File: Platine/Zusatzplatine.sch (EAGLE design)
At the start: 23 parts

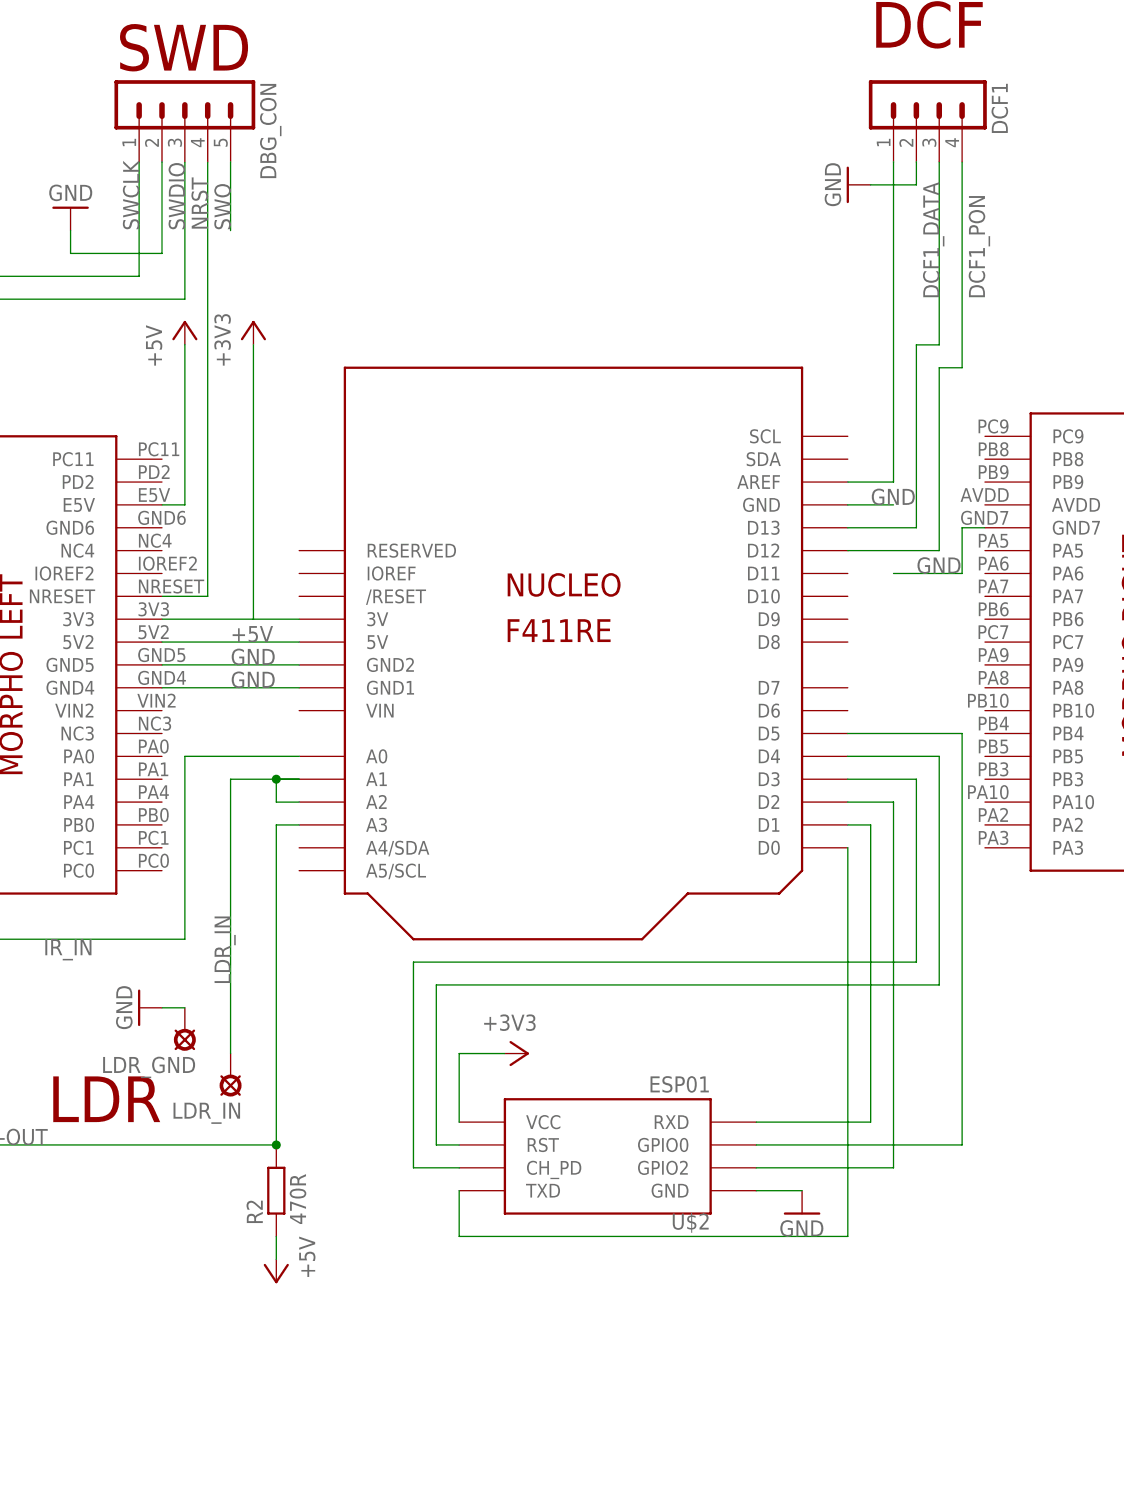
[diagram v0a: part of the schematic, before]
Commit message: Added Upside Down Mount Option for WiFI Improved Documentation on Board
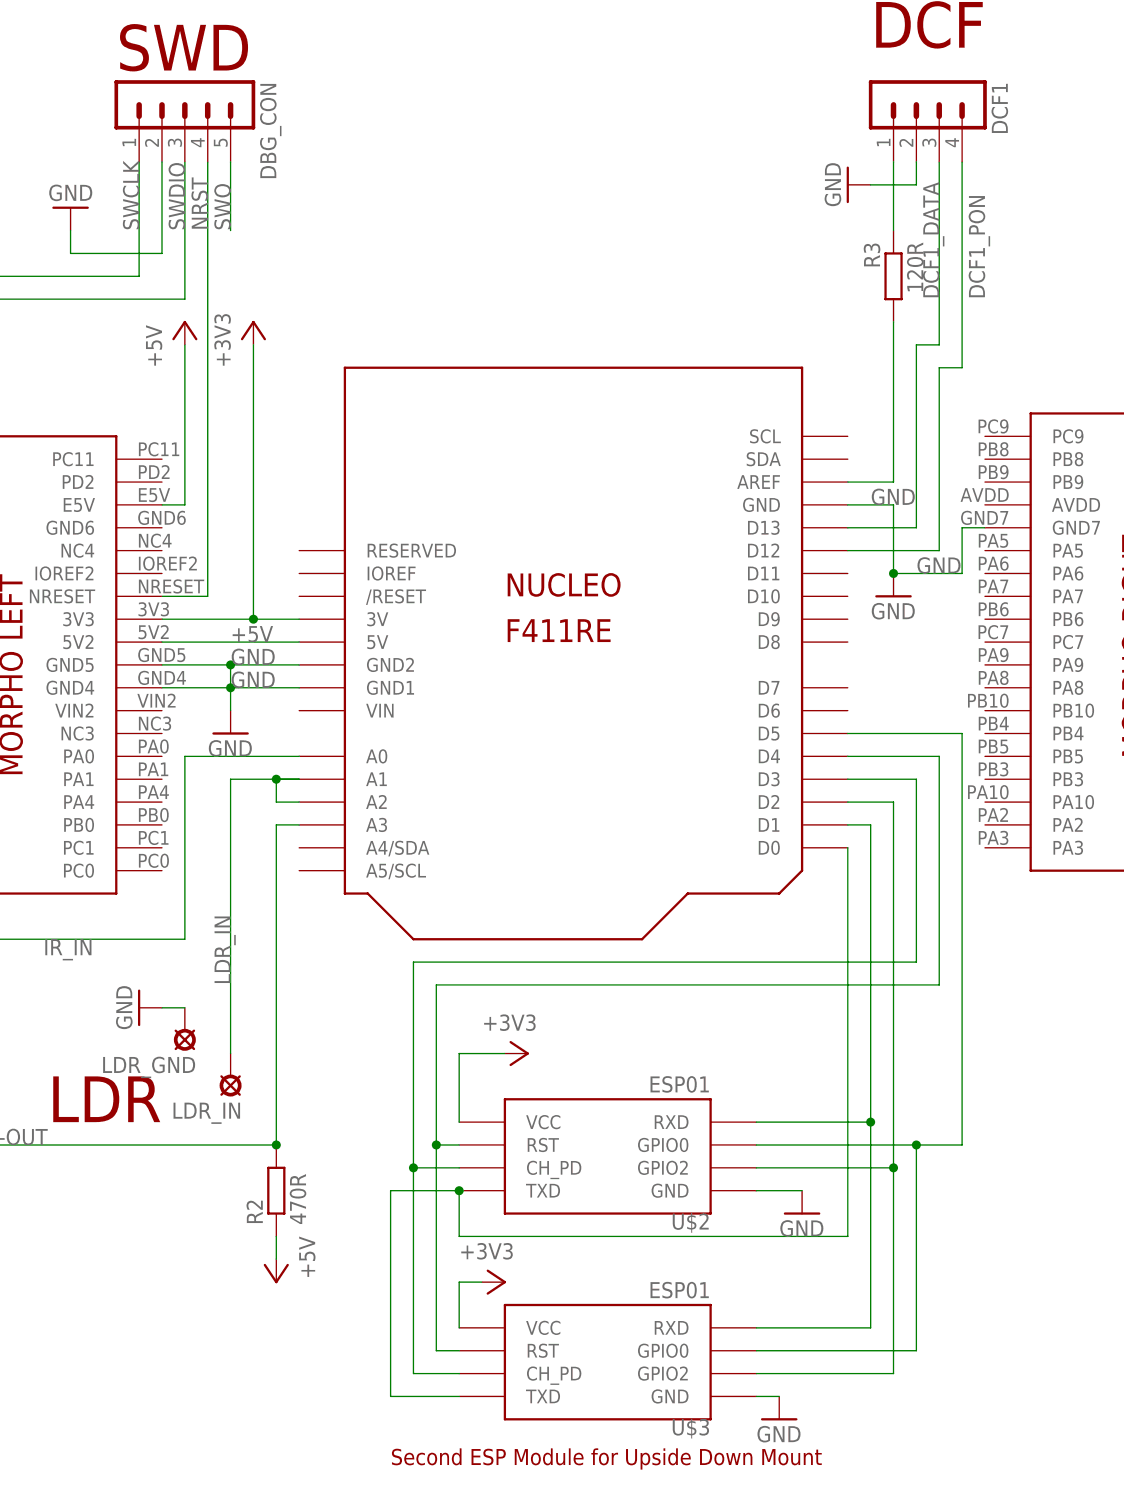
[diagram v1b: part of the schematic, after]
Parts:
- added R3: 120R, rcl:R-EU_R1206
- added U$3: ESP01, esp8266modules:ESP01
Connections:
- new net N$2: DCF1.1, R3.1
- net +3V3: now also U$3.VCC
- net GND: now also U$3.GND
- net N$1: now also R3.2; no longer DCF1.1
- net N$12: now also U$3.GPIO0
- net N$13: now also U$3.RST
- net N$14: now also U$3.CH_PD
- net N$15: now also U$3.TXD
- net N$16: now also U$3.RXD
- net N$17: now also U$3.GPIO2
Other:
- note added: "Second ESP Module for Upside Down Mount"
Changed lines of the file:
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@@
 <part name="GND6" library="supply1" deviceset="GND" device=""/>
 <part name="3V3" library="supply1" deviceset="+3V3" device=""/>
+<part name="U$3" library="esp8266modules" deviceset="ESP01" device=""/>
+<part name="3V4" library="supply1" deviceset="+3V3" device=""/>
+<part name="GND7" library="supply1" deviceset="GND" device=""/>
+<part name="GND8" library="supply1" deviceset="GND" device=""/>
+<part name="GND9" library="supply1" deviceset="GND" device=""/>
+<part name="R3" library="rcl" deviceset="R-EU_" device="R1206" value="120R"/>
 </parts>
 <sheets>
@@
 <text x="-50.8" y="-165.1" size="5.08" layer="94">IR</text>
 <text x="-20.32" y="-48.26" size="5.08" layer="94">SWD</text>
+<text x="10.16" y="-203.2" size="1.778" layer="94">Second ESP Module for Upside Down Mount</text>
 </plain>
 <instances>
@@
 <instance part="GND6" gate="1" x="-25.4" y="-63.5" rot="R180"/>
 <instance part="3V3" gate="G$1" x="25.4" y="-157.48" rot="R270"/>
+<instance part="U$3" gate="G$1" x="33.02" y="-187.96" rot="R180"/>
+<instance part="3V4" gate="G$1" x="22.86" y="-182.88" rot="R270"/>
+<instance part="GND7" gate="1" x="53.34" y="-198.12"/>
+<instance part="GND8" gate="1" x="-7.62" y="-121.92"/>
+<instance part="GND9" gate="1" x="66.04" y="-106.68"/>
+<instance part="R3" gate="G$1" x="66.04" y="-71.12" rot="MR270"/>
 </instances>
 <busses>
@@
 </segment>
 <segment>
+<pinref part="U$1" gate="G$1" pin="GND1"/>
+<pinref part="U$1" gate="G$1" pin="GND4"/>
+<wire x1="0" y1="-116.84" x2="-7.62" y2="-116.84" width="0.1524" layer="91"/>
+<label x="-7.62" y="-116.84" size="1.778" layer="95"/>
+<pinref part="GND8" gate="1" pin="GND"/>
+<wire x1="-7.62" y1="-116.84" x2="-15.24" y2="-116.84" width="0.1524" layer="91"/>
+<wire x1="-7.62" y1="-119.38" x2="-7.62" y2="-116.84" width="0.1524" layer="91"/>
 <pinref part="U$1" gate="G$1" pin="GND2"/>
 <pinref part="U$1" gate="G$1" pin="GND5"/>
-<wire x1="0" y1="-114.3" x2="-15.24" y2="-114.3" width="0.1524" layer="91"/>
+<wire x1="0" y1="-114.3" x2="-7.62" y2="-114.3" width="0.1524" layer="91"/>
 <label x="-7.62" y="-114.3" size="1.778" layer="95"/>
-</segment>
-<segment>
-<pinref part="U$1" gate="G$1" pin="GND1"/>
-<pinref part="U$1" gate="G$1" pin="GND4"/>
-<wire x1="0" y1="-116.84" x2="-15.24" y2="-116.84" width="0.1524" layer="91"/>
-<label x="-7.62" y="-116.84" size="1.778" layer="95"/>
+<wire x1="-7.62" y1="-114.3" x2="-15.24" y2="-114.3" width="0.1524" layer="91"/>
+<wire x1="-7.62" y1="-116.84" x2="-7.62" y2="-114.3" width="0.1524" layer="91"/>
+<junction x="-7.62" y="-116.84"/>
+<junction x="-7.62" y="-114.3"/>
 </segment>
 <segment>
@@
 <wire x1="73.66" y1="-104.14" x2="66.04" y2="-104.14" width="0.1524" layer="91"/>
 <label x="68.58" y="-104.14" size="1.778" layer="95"/>
-</segment>
-<segment>
+<pinref part="GND9" gate="1" pin="GND"/>
 <pinref part="U$1" gate="G$1" pin="GND"/>
 <wire x1="60.96" y1="-96.52" x2="66.04" y2="-96.52" width="0.1524" layer="91"/>
 <label x="63.5" y="-96.52" size="1.778" layer="95"/>
+<wire x1="66.04" y1="-96.52" x2="66.04" y2="-104.14" width="0.1524" layer="91"/>
+<junction x="66.04" y="-104.14"/>
+</segment>
+<segment>
+<pinref part="U$3" gate="G$1" pin="GND"/>
+<pinref part="GND7" gate="1" pin="GND"/>
+<wire x1="50.8" y1="-195.58" x2="53.34" y2="-195.58" width="0.1524" layer="91"/>
 </segment>
 </net>
@@
 <segment>
 <pinref part="U$2" gate="G$1" pin="GPIO0"/>
-<wire x1="50.8" y1="-167.64" x2="73.66" y2="-167.64" width="0.1524" layer="91"/>
+<wire x1="50.8" y1="-167.64" x2="68.58" y2="-167.64" width="0.1524" layer="91"/>
+<wire x1="68.58" y1="-167.64" x2="73.66" y2="-167.64" width="0.1524" layer="91"/>
 <wire x1="73.66" y1="-167.64" x2="73.66" y2="-121.92" width="0.1524" layer="91"/>
 <pinref part="U$1" gate="G$1" pin="D5"/>
 <wire x1="73.66" y1="-121.92" x2="60.96" y2="-121.92" width="0.1524" layer="91"/>
+<pinref part="U$3" gate="G$1" pin="GPIO0"/>
+<wire x1="50.8" y1="-190.5" x2="68.58" y2="-190.5" width="0.1524" layer="91"/>
+<wire x1="68.58" y1="-190.5" x2="68.58" y2="-167.64" width="0.1524" layer="91"/>
+<junction x="68.58" y="-167.64"/>
 </segment>
 </net>
@@
 <pinref part="U$1" gate="G$1" pin="D4"/>
 <wire x1="71.12" y1="-124.46" x2="60.96" y2="-124.46" width="0.1524" layer="91"/>
+<wire x1="15.24" y1="-167.64" x2="15.24" y2="-190.5" width="0.1524" layer="91"/>
+<pinref part="U$3" gate="G$1" pin="RST"/>
+<wire x1="15.24" y1="-190.5" x2="17.78" y2="-190.5" width="0.1524" layer="91"/>
+<junction x="15.24" y="-167.64"/>
 </segment>
 </net>
@@
 <pinref part="U$1" gate="G$1" pin="D3"/>
 <wire x1="68.58" y1="-127" x2="60.96" y2="-127" width="0.1524" layer="91"/>
+<wire x1="12.7" y1="-170.18" x2="12.7" y2="-193.04" width="0.1524" layer="91"/>
+<pinref part="U$3" gate="G$1" pin="CH_PD"/>
+<wire x1="12.7" y1="-193.04" x2="17.78" y2="-193.04" width="0.1524" layer="91"/>
+<junction x="12.7" y="-170.18"/>
 </segment>
 </net>
@@
 <wire x1="17.78" y1="-177.8" x2="60.96" y2="-177.8" width="0.1524" layer="91"/>
 <wire x1="60.96" y1="-177.8" x2="60.96" y2="-134.62" width="0.1524" layer="91"/>
+<pinref part="U$3" gate="G$1" pin="TXD"/>
+<wire x1="17.78" y1="-195.58" x2="10.16" y2="-195.58" width="0.1524" layer="91"/>
+<wire x1="10.16" y1="-195.58" x2="10.16" y2="-172.72" width="0.1524" layer="91"/>
+<wire x1="10.16" y1="-172.72" x2="17.78" y2="-172.72" width="0.1524" layer="91"/>
+<junction x="17.78" y="-172.72"/>
 </segment>
 </net>
@@
 <pinref part="U$2" gate="G$1" pin="RXD"/>
 <wire x1="63.5" y1="-165.1" x2="50.8" y2="-165.1" width="0.1524" layer="91"/>
+<pinref part="U$3" gate="G$1" pin="RXD"/>
+<wire x1="50.8" y1="-187.96" x2="63.5" y2="-187.96" width="0.1524" layer="91"/>
+<wire x1="63.5" y1="-187.96" x2="63.5" y2="-165.1" width="0.1524" layer="91"/>
+<junction x="63.5" y="-165.1"/>
 </segment>
 </net>
@@
 <pinref part="U$1" gate="G$1" pin="D2"/>
 <wire x1="66.04" y1="-129.54" x2="60.96" y2="-129.54" width="0.1524" layer="91"/>
+<pinref part="U$3" gate="G$1" pin="GPIO2"/>
+<wire x1="50.8" y1="-193.04" x2="66.04" y2="-193.04" width="0.1524" layer="91"/>
+<wire x1="66.04" y1="-193.04" x2="66.04" y2="-170.18" width="0.1524" layer="91"/>
+<junction x="66.04" y="-170.18"/>
 </segment>
 </net>
@@
 <net name="N$1" class="0">
 <segment>
-<pinref part="DCF1" gate="1" pin="1"/>
-<wire x1="66.04" y1="-58.42" x2="66.04" y2="-93.98" width="0.1524" layer="91"/>
 <pinref part="U$1" gate="G$1" pin="AREF"/>
 <wire x1="66.04" y1="-93.98" x2="60.96" y2="-93.98" width="0.1524" layer="91"/>
+<pinref part="R3" gate="G$1" pin="2"/>
+<wire x1="66.04" y1="-76.2" x2="66.04" y2="-93.98" width="0.1524" layer="91"/>
 </segment>
 </net>
@@
 <pinref part="U$1" gate="G$1" pin="3V"/>
 <wire x1="-5.08" y1="-109.22" x2="0" y2="-109.22" width="0.1524" layer="91"/>
+<junction x="-5.08" y="-109.22"/>
 </segment>
 <segment>
@@
 <pinref part="3V3" gate="G$1" pin="+3V3"/>
 <wire x1="17.78" y1="-157.48" x2="22.86" y2="-157.48" width="0.1524" layer="91"/>
+</segment>
+<segment>
+<pinref part="U$3" gate="G$1" pin="VCC"/>
+<wire x1="17.78" y1="-187.96" x2="17.78" y2="-182.88" width="0.1524" layer="91"/>
+<pinref part="3V4" gate="G$1" pin="+3V3"/>
+<wire x1="17.78" y1="-182.88" x2="20.32" y2="-182.88" width="0.1524" layer="91"/>
 </segment>
 </net>
@@
 </segment>
 </net>
+<net name="N$2" class="0">
+<segment>
+<pinref part="DCF1" gate="1" pin="1"/>
+<pinref part="R3" gate="G$1" pin="1"/>
+<wire x1="66.04" y1="-58.42" x2="66.04" y2="-66.04" width="0.1524" layer="91"/>
+</segment>
+</net>

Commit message: - DCF-Leitungen umgelegt - Doku korrigiert
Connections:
- net DCF1_DATA: now also U$1.SCL; no longer U$1.D13
- net DCF1_PON: now also U$1.SDA; no longer U$1.D12
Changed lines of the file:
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@@
 <?xml version="1.0" encoding="utf-8"?>
 <!DOCTYPE eagle SYSTEM "eagle.dtd">
-<eagle version="7.2.0">
+<eagle version="7.4.0">
 <drawing>
 <settings>
@@
 <wire x1="73.66" y1="-58.42" x2="73.66" y2="-81.28" width="0.1524" layer="91"/>
 <wire x1="73.66" y1="-81.28" x2="71.12" y2="-81.28" width="0.1524" layer="91"/>
-<wire x1="71.12" y1="-81.28" x2="71.12" y2="-101.6" width="0.1524" layer="91"/>
 <label x="76.2" y="-73.66" size="1.778" layer="95" rot="R90"/>
-<pinref part="U$1" gate="G$1" pin="D12"/>
-<wire x1="71.12" y1="-101.6" x2="60.96" y2="-101.6" width="0.1524" layer="91"/>
+<wire x1="71.12" y1="-81.28" x2="71.12" y2="-91.44" width="0.1524" layer="91"/>
+<pinref part="U$1" gate="G$1" pin="SDA"/>
+<wire x1="71.12" y1="-91.44" x2="60.96" y2="-91.44" width="0.1524" layer="91"/>
 </segment>
 </net>
@@
 <pinref part="DCF1" gate="1" pin="3"/>
 <label x="71.12" y="-73.66" size="1.778" layer="95" rot="R90"/>
-<wire x1="60.96" y1="-99.06" x2="68.58" y2="-99.06" width="0.1524" layer="91"/>
-<wire x1="68.58" y1="-99.06" x2="68.58" y2="-78.74" width="0.1524" layer="91"/>
 <wire x1="68.58" y1="-78.74" x2="71.12" y2="-78.74" width="0.1524" layer="91"/>
 <wire x1="71.12" y1="-78.74" x2="71.12" y2="-58.42" width="0.1524" layer="91"/>
-<pinref part="U$1" gate="G$1" pin="D13"/>
-</segment>
-</net>
+<wire x1="68.58" y1="-78.74" x2="68.58" y2="-88.9" width="0.1524" layer="91"/>
+<pinref part="U$1" gate="G$1" pin="SCL"/>
+<wire x1="68.58" y1="-88.9" x2="60.96" y2="-88.9" width="0.1524" layer="91"/>
+</segment>
+</net>
